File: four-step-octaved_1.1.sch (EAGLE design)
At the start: 39 parts, among them IC1 556, IC2 4017N, IC3 4040N, J1 BATTERY, J2 SPEAKER, U1 LM386N

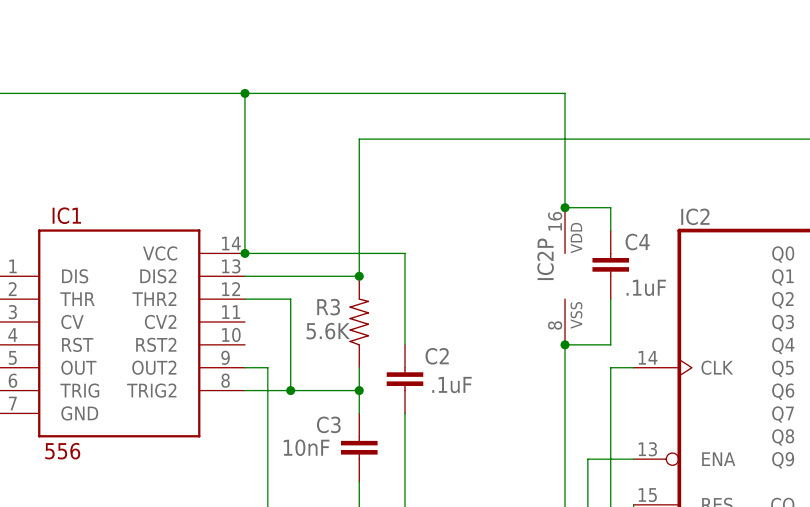
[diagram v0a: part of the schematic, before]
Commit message: Fix missing 556 pin10 on both schematics
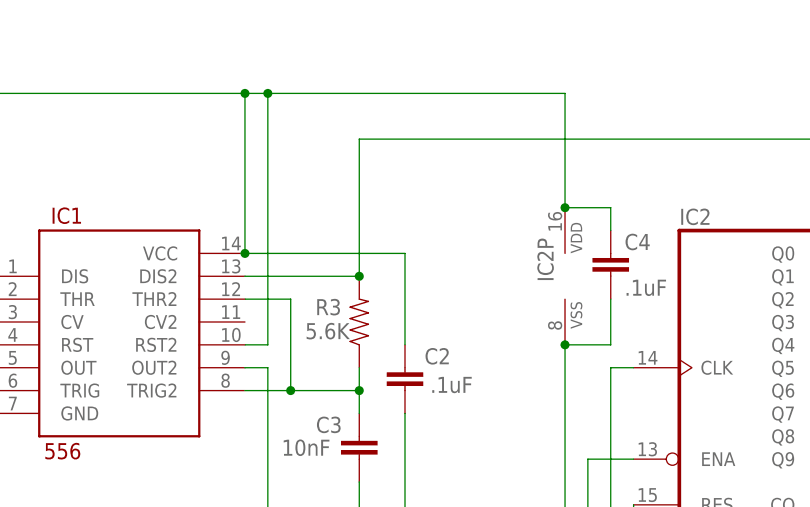
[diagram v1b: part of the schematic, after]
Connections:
- net +9V: now also IC1.RST2
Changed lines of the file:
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@@
 <wire x1="43.18" y1="88.9" x2="43.18" y2="78.74" width="0.1524" layer="91"/>
 <junction x="25.4" y="88.9"/>
-<wire x1="25.4" y1="106.68" x2="60.96" y2="106.68" width="0.1524" layer="91"/>
+<wire x1="25.4" y1="106.68" x2="27.94" y2="106.68" width="0.1524" layer="91"/>
 <junction x="25.4" y="106.68"/>
 <pinref part="IC2" gate="P" pin="VDD"/>
+<wire x1="27.94" y1="106.68" x2="60.96" y2="106.68" width="0.1524" layer="91"/>
 <wire x1="60.96" y1="106.68" x2="60.96" y2="93.98" width="0.1524" layer="91"/>
 <pinref part="C4" gate="G$1" pin="1"/>
@@
 <wire x1="-43.18" y1="93.98" x2="-43.18" y2="93.345" width="0.1524" layer="91"/>
 <junction x="-38.1" y="93.98"/>
+<pinref part="IC1" gate="G$1" pin="RST2"/>
+<wire x1="25.4" y1="78.74" x2="27.94" y2="78.74" width="0.1524" layer="91"/>
+<wire x1="27.94" y1="78.74" x2="27.94" y2="106.68" width="0.1524" layer="91"/>
+<junction x="27.94" y="106.68"/>
 </segment>
 </net>

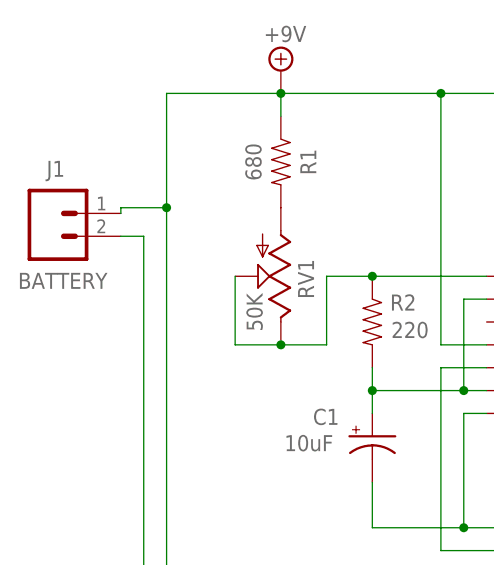
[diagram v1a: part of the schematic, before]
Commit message: Fix text on wrong layer, only on 1.1
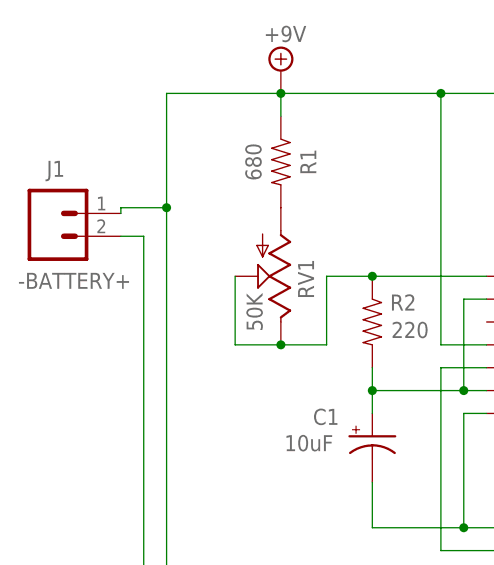
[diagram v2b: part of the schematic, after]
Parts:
- J1: value BATTERY -> -BATTERY+
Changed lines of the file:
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@@
 <part name="C6" library="SparkFun-Capacitors" deviceset="100UF-POLAR" device="-RADIAL-2.5MM-25V-20%" value="220uF"/>
 <part name="J2" library="SparkFun-Connectors" deviceset="CONN_02" device="" value="SPEAKER"/>
-<part name="J1" library="SparkFun-Connectors" deviceset="CONN_02" device="" value="BATTERY"/>
+<part name="J1" library="SparkFun-Connectors" deviceset="CONN_02" device="" value="-BATTERY+"/>
 <part name="R11" library="SparkFun-Resistors" deviceset="1KOHM" device="-HORIZ-1/4W-1%" value="22K"/>
 <part name="R12" library="SparkFun-Resistors" deviceset="1KOHM" device="-HORIZ-1/4W-1%" value="22K"/>

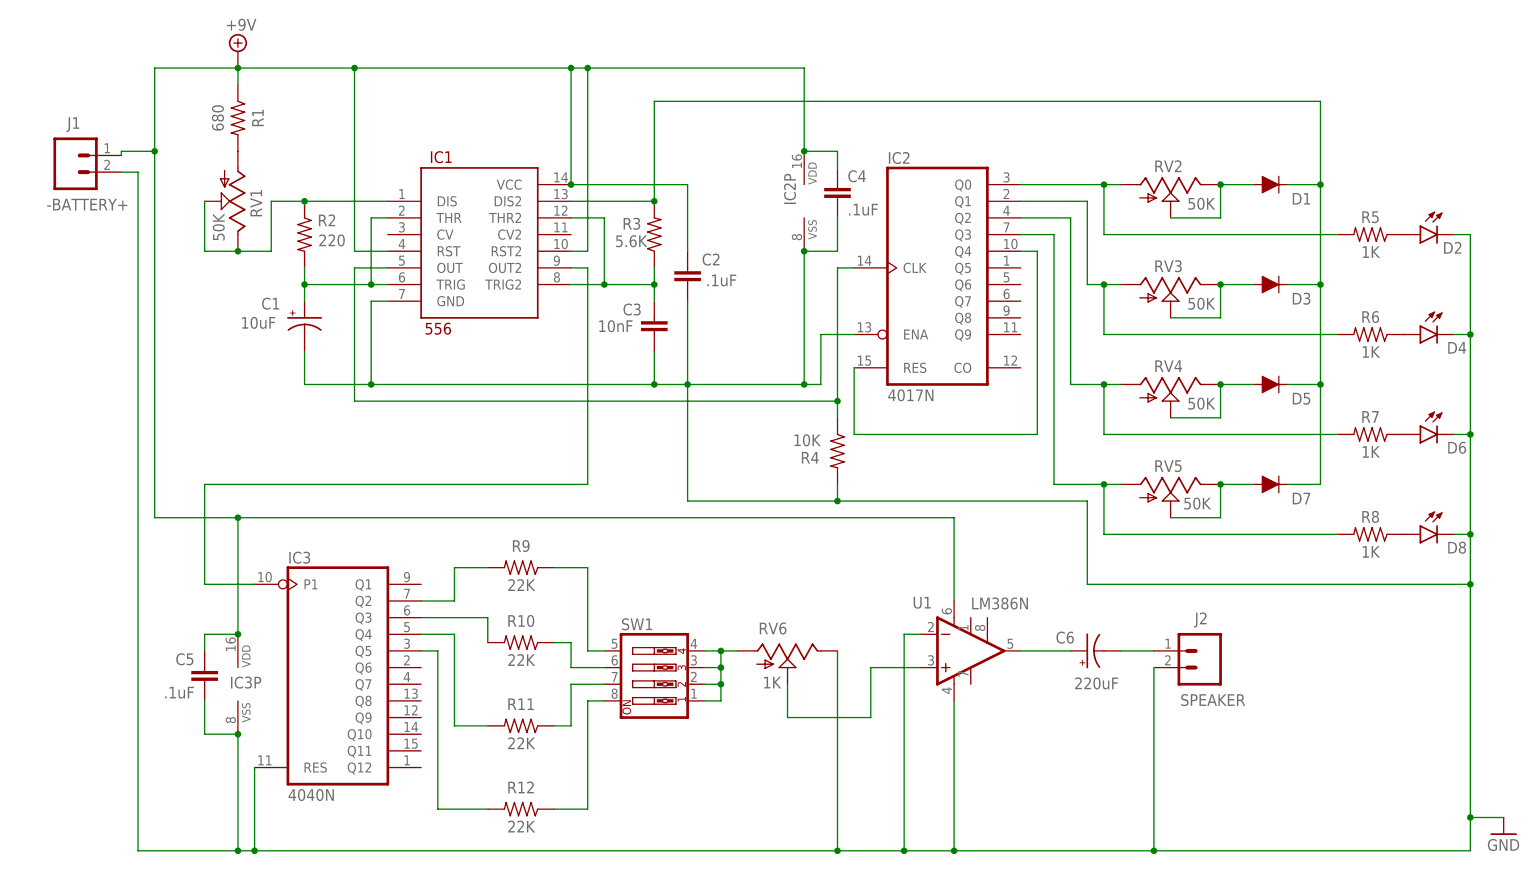
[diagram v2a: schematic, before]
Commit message: Rename RV to VR to match waltron
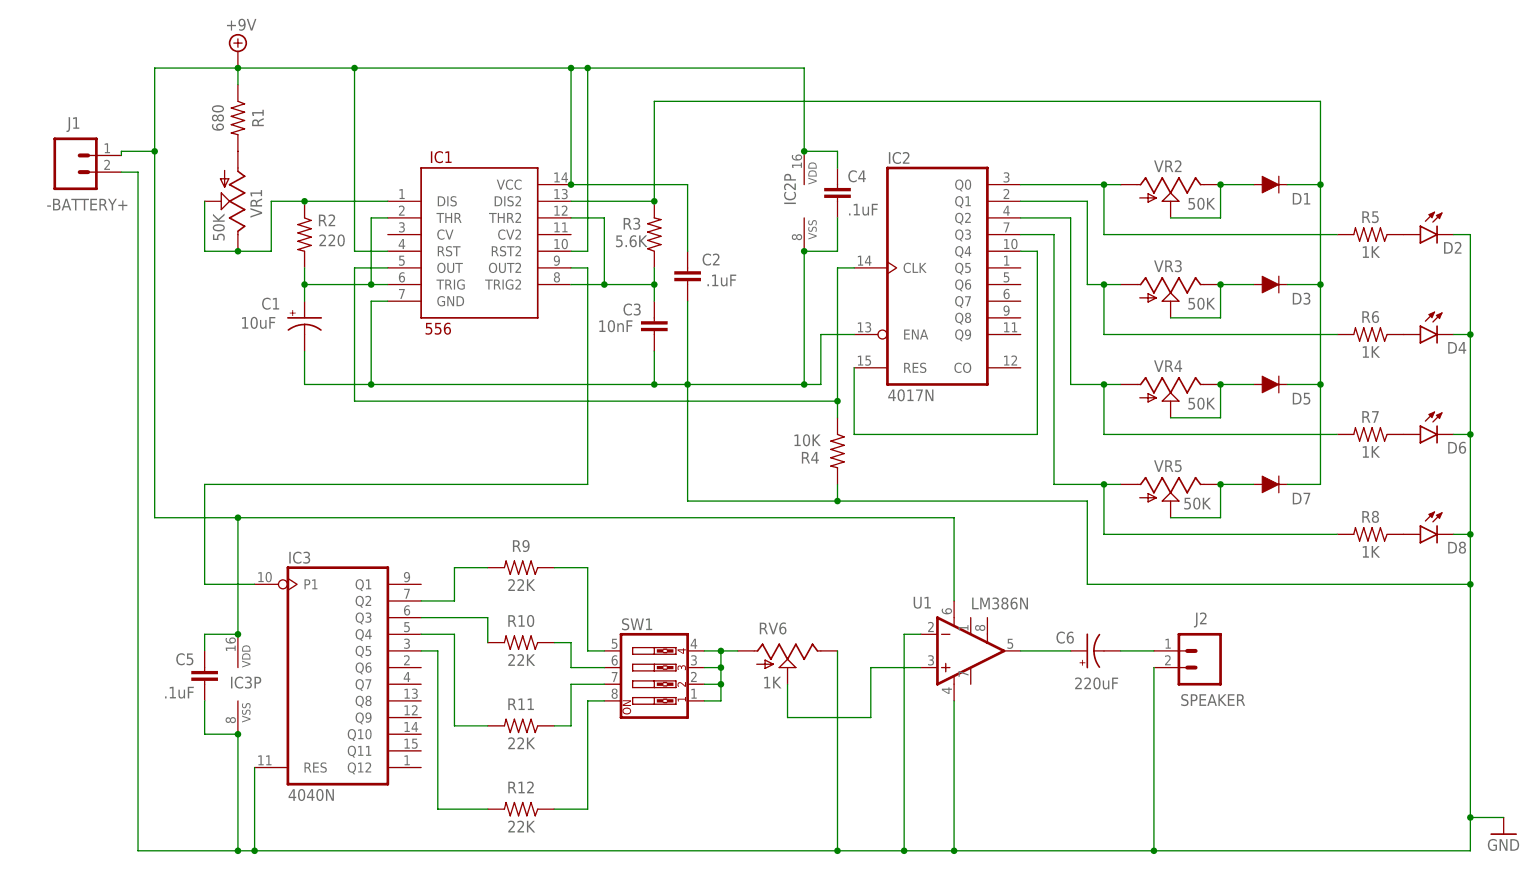
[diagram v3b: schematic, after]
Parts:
- renumbered RV1 to VR1, RV2 to VR2, RV3 to VR3, RV4 to VR4, RV5 to VR5
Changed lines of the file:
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@@
 <part name="R2" library="SparkFun-Resistors" deviceset="1KOHM" device="-HORIZ-1/4W-1%" value="220"/>
 <part name="R3" library="SparkFun-Resistors" deviceset="1KOHM" device="-HORIZ-1/4W-1%" value="5.6K"/>
-<part name="RV1" library="SparkFun-Retired" deviceset="POT" device="TRIM" value="50K"/>
+<part name="VR1" library="SparkFun-Retired" deviceset="POT" device="TRIM" value="50K"/>
 <part name="C1" library="SparkFun-Capacitors" deviceset="10UF-POLAR" device="-RADIAL-2.5MM-25V-20%" value="10uF"/>
 <part name="C2" library="SparkFun-Capacitors" deviceset="0.1UF" device="-KIT-EZ-50V-20%" value=".1uF"/>
@@
 <part name="R8" library="SparkFun-Resistors" deviceset="1KOHM" device="-HORIZ-1/4W-1%" value="1K"/>
 <part name="D2" library="SparkFun-LED" deviceset="LED" device="3MM"/>
-<part name="RV2" library="SparkFun-Retired" deviceset="POT" device="TRIM" value="50K"/>
-<part name="RV3" library="SparkFun-Retired" deviceset="POT" device="TRIM" value="50K"/>
-<part name="RV4" library="SparkFun-Retired" deviceset="POT" device="TRIM" value="50K"/>
-<part name="RV5" library="SparkFun-Retired" deviceset="POT" device="TRIM" value="50K"/>
+<part name="VR2" library="SparkFun-Retired" deviceset="POT" device="TRIM" value="50K"/>
+<part name="VR3" library="SparkFun-Retired" deviceset="POT" device="TRIM" value="50K"/>
+<part name="VR4" library="SparkFun-Retired" deviceset="POT" device="TRIM" value="50K"/>
+<part name="VR5" library="SparkFun-Retired" deviceset="POT" device="TRIM" value="50K"/>
 <part name="D1" library="SparkFun-DiscreteSemi" deviceset="DIODE" device="-PTH" value=""/>
 <part name="D3" library="SparkFun-DiscreteSemi" deviceset="DIODE" device="-PTH" value=""/>
@@
 <attribute name="VALUE" x="34.544" y="79.375" size="1.778" layer="96" font="vector" rot="R180" align="top-center"/>
 </instance>
-<instance part="RV1" gate="G$1" x="-25.4" y="86.36" smashed="yes" rot="R180">
+<instance part="VR1" gate="G$1" x="-25.4" y="86.36" smashed="yes" rot="R180">
 <attribute name="NAME" x="-23.495" y="88.265" size="1.778" layer="95" rot="R270"/>
 <attribute name="VALUE" x="-29.21" y="84.455" size="1.778" layer="95" rot="R270"/>
@@
 <attribute name="VALUE" x="159.512" y="79.375" size="1.778" layer="96" font="vector" rot="MR0" align="top-left"/>
 </instance>
-<instance part="RV2" gate="G$1" x="116.84" y="88.9" smashed="yes" rot="R270">
+<instance part="VR2" gate="G$1" x="116.84" y="88.9" smashed="yes" rot="R270">
 <attribute name="NAME" x="114.3" y="90.805" size="1.778" layer="95"/>
 <attribute name="VALUE" x="119.38" y="85.09" size="1.778" layer="95"/>
 </instance>
-<instance part="RV3" gate="G$1" x="116.84" y="73.66" smashed="yes" rot="R270">
+<instance part="VR3" gate="G$1" x="116.84" y="73.66" smashed="yes" rot="R270">
 <attribute name="NAME" x="114.3" y="75.565" size="1.778" layer="95"/>
 <attribute name="VALUE" x="119.38" y="69.85" size="1.778" layer="95"/>
 </instance>
-<instance part="RV4" gate="G$1" x="116.84" y="58.42" smashed="yes" rot="R270">
+<instance part="VR4" gate="G$1" x="116.84" y="58.42" smashed="yes" rot="R270">
 <attribute name="NAME" x="114.3" y="60.325" size="1.778" layer="95"/>
 <attribute name="VALUE" x="119.38" y="54.61" size="1.778" layer="95"/>
 </instance>
-<instance part="RV5" gate="G$1" x="116.84" y="43.18" smashed="yes" rot="R270">
+<instance part="VR5" gate="G$1" x="116.84" y="43.18" smashed="yes" rot="R270">
 <attribute name="NAME" x="114.3" y="45.085" size="1.778" layer="95"/>
 <attribute name="VALUE" x="118.745" y="39.37" size="1.778" layer="95"/>
@@
 <segment>
 <pinref part="R1" gate="G$1" pin="2"/>
-<pinref part="RV1" gate="G$1" pin="A"/>
+<pinref part="VR1" gate="G$1" pin="A"/>
 </segment>
 </net>
@@
 <segment>
 <pinref part="IC1" gate="G$1" pin="DIS"/>
-<pinref part="RV1" gate="G$1" pin="E"/>
+<pinref part="VR1" gate="G$1" pin="E"/>
 <wire x1="-2.54" y1="86.36" x2="-15.24" y2="86.36" width="0.1524" layer="91"/>
 <wire x1="-15.24" y1="86.36" x2="-20.32" y2="86.36" width="0.1524" layer="91"/>
@@
 <wire x1="-25.4" y1="78.74" x2="-30.48" y2="78.74" width="0.1524" layer="91"/>
 <junction x="-25.4" y="78.74"/>
-<pinref part="RV1" gate="G$1" pin="S"/>
+<pinref part="VR1" gate="G$1" pin="S"/>
 <wire x1="-30.48" y1="78.74" x2="-30.48" y2="86.36" width="0.1524" layer="91"/>
 <pinref part="R2" gate="G$1" pin="1"/>
@@
 <wire x1="93.98" y1="83.82" x2="101.6" y2="83.82" width="0.1524" layer="91"/>
 <wire x1="101.6" y1="83.82" x2="101.6" y2="58.42" width="0.1524" layer="91"/>
-<pinref part="RV4" gate="G$1" pin="A"/>
+<pinref part="VR4" gate="G$1" pin="A"/>
 <wire x1="109.22" y1="58.42" x2="106.68" y2="58.42" width="0.1524" layer="91"/>
 <wire x1="106.68" y1="58.42" x2="101.6" y2="58.42" width="0.1524" layer="91"/>
@@
 <wire x1="93.98" y1="81.28" x2="99.06" y2="81.28" width="0.1524" layer="91"/>
 <wire x1="99.06" y1="81.28" x2="99.06" y2="43.18" width="0.1524" layer="91"/>
-<pinref part="RV5" gate="G$1" pin="A"/>
+<pinref part="VR5" gate="G$1" pin="A"/>
 <wire x1="109.22" y1="43.18" x2="106.68" y2="43.18" width="0.1524" layer="91"/>
 <wire x1="106.68" y1="43.18" x2="99.06" y2="43.18" width="0.1524" layer="91"/>
@@
 <segment>
 <pinref part="IC2" gate="A" pin="Q0"/>
-<pinref part="RV2" gate="G$1" pin="A"/>
+<pinref part="VR2" gate="G$1" pin="A"/>
 <wire x1="93.98" y1="88.9" x2="106.68" y2="88.9" width="0.1524" layer="91"/>
 <wire x1="106.68" y1="88.9" x2="109.22" y2="88.9" width="0.1524" layer="91"/>
@@
 <wire x1="93.98" y1="86.36" x2="104.14" y2="86.36" width="0.1524" layer="91"/>
 <wire x1="104.14" y1="86.36" x2="104.14" y2="73.66" width="0.1524" layer="91"/>
-<pinref part="RV3" gate="G$1" pin="A"/>
+<pinref part="VR3" gate="G$1" pin="A"/>
 <wire x1="104.14" y1="73.66" x2="106.68" y2="73.66" width="0.1524" layer="91"/>
 <wire x1="106.68" y1="73.66" x2="109.22" y2="73.66" width="0.1524" layer="91"/>
@@
 <net name="N$11" class="1">
 <segment>
-<pinref part="RV2" gate="G$1" pin="S"/>
-<pinref part="RV2" gate="G$1" pin="E"/>
+<pinref part="VR2" gate="G$1" pin="S"/>
+<pinref part="VR2" gate="G$1" pin="E"/>
 <wire x1="116.84" y1="83.82" x2="124.46" y2="83.82" width="0.1524" layer="91"/>
 <wire x1="124.46" y1="83.82" x2="124.46" y2="88.9" width="0.1524" layer="91"/>
@@
 <net name="N$16" class="1">
 <segment>
-<pinref part="RV3" gate="G$1" pin="S"/>
-<pinref part="RV3" gate="G$1" pin="E"/>
+<pinref part="VR3" gate="G$1" pin="S"/>
+<pinref part="VR3" gate="G$1" pin="E"/>
 <wire x1="116.84" y1="68.58" x2="124.46" y2="68.58" width="0.1524" layer="91"/>
 <wire x1="124.46" y1="68.58" x2="124.46" y2="73.66" width="0.1524" layer="91"/>
@@
 <net name="N$18" class="1">
 <segment>
-<pinref part="RV5" gate="G$1" pin="S"/>
-<pinref part="RV5" gate="G$1" pin="E"/>
+<pinref part="VR5" gate="G$1" pin="S"/>
+<pinref part="VR5" gate="G$1" pin="E"/>
 <wire x1="116.84" y1="38.1" x2="124.46" y2="38.1" width="0.1524" layer="91"/>
 <wire x1="124.46" y1="38.1" x2="124.46" y2="43.18" width="0.1524" layer="91"/>
@@
 <net name="N$17" class="1">
 <segment>
-<pinref part="RV4" gate="G$1" pin="S"/>
-<pinref part="RV4" gate="G$1" pin="E"/>
+<pinref part="VR4" gate="G$1" pin="S"/>
+<pinref part="VR4" gate="G$1" pin="E"/>
 <wire x1="116.84" y1="53.34" x2="124.46" y2="53.34" width="0.1524" layer="91"/>
 <wire x1="124.46" y1="53.34" x2="124.46" y2="58.42" width="0.1524" layer="91"/>
